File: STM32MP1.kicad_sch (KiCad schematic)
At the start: 1 part, among them U2 EMMC04G-S100-B08U

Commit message: added mmc schematic
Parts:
- removed U2: EMMC04G-S100-B08U, EMMC04G-S100-B08U:MICRON_EMMC_153-12, symbol EMMC04G-S100-B08U:EMMC04G-S100-B08U
- added J1: Micro_SD_Card_Det1, microSD:J_SD_Card-micro_socket_A, symbol Connector:Micro_SD_Card_Det1
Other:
- added sheet EMMC (EMMC.kicad_sch)
- sheet STM32MP1_Processor ports: added EMMC[0..10], GND, VDD_DDR, VREF_DDR; removed none

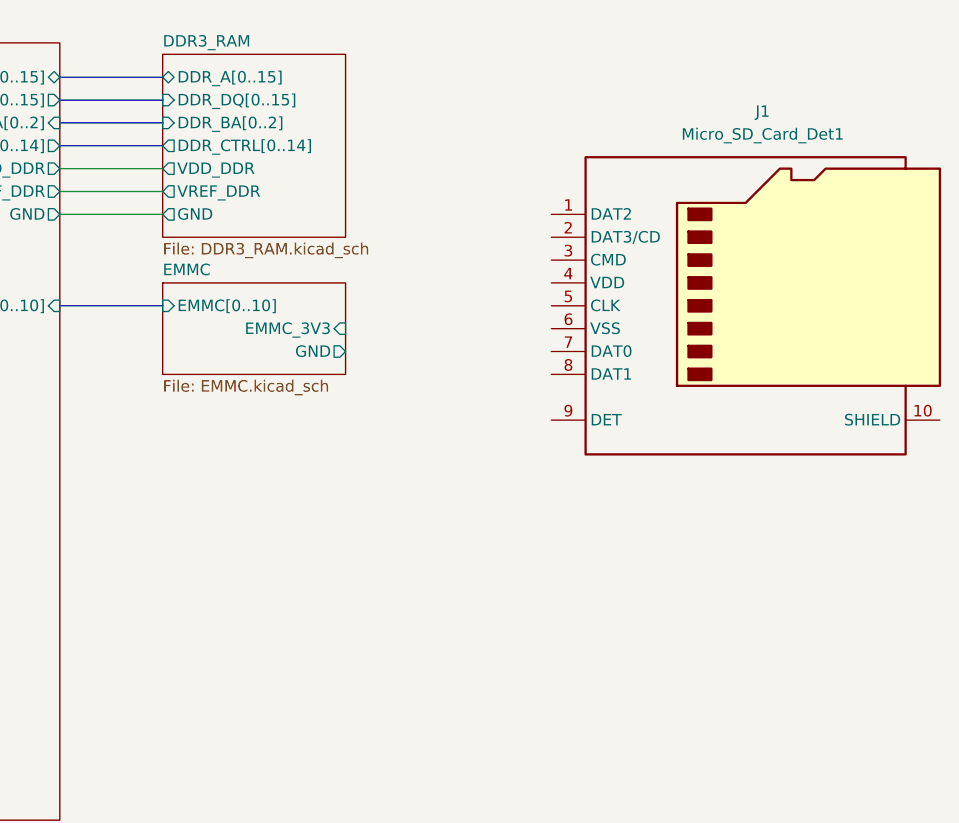
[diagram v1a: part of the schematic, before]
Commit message: Included Tushar's changed also added SDCARD module
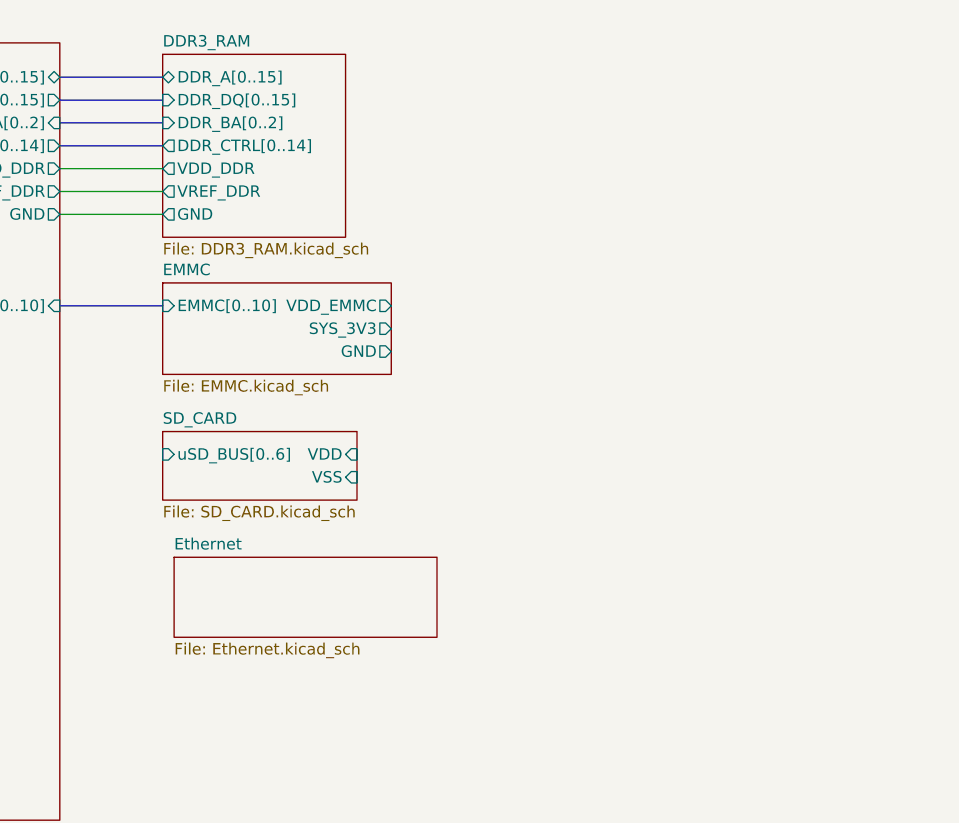
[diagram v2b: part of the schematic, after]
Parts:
- removed J1: Micro_SD_Card_Det1, microSD:J_SD_Card-micro_socket_A, symbol Connector:Micro_SD_Card_Det1
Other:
- added sheet Ethernet (Ethernet.kicad_sch)
- added sheet SD_CARD (SD_CARD.kicad_sch)
- sheet EMMC ports: added SYS_3V3, VDD_EMMC; removed EMMC_3V3
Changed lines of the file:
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@@
-		)
-	)
-	(symbol
-		(lib_id "Connector:Micro_SD_Card_Det1")
-		(at 214.63 67.31 0)
-		(unit 1)
-		(exclude_from_sim no)
-		(in_bom yes)
-		(on_board yes)
-		(dnp no)
-		(fields_autoplaced yes)
-		(property "Reference" "J1"
-			(at 215.265 45.72 0)
-			(effects
-				(font
-					(size 1.27 1.27)
-				)
-			)
-		)
-		(property "Value" "Micro_SD_Card_Det1"
-			(at 215.265 48.26 0)
-			(effects
-				(font
-					(size 1.27 1.27)
-				)
-			)
-		)
-		(property "Footprint" "microSD:J_SD_Card-micro_socket_A"
-			(at 266.7 49.53 0)
-			(effects
-				(font
-					(size 1.27 1.27)
-				)
-				(hide yes)
-			)
-		)
-		(property "Datasheet" "https://datasheet.lcsc.com/lcsc/2110151630_XKB-Connectivity-XKTF-015-N_C381082.pdf"
-			(at 214.63 64.77 0)
-			(effects
-				(font
-					(size 1.27 1.27)
-				)
-				(hide yes)
-			)
-		)
-		(property "Description" "Micro SD Card Socket with one card detection pin"
-			(at 214.63 67.31 0)
-			(effects
-				(font
-					(size 1.27 1.27)
-				)
-				(hide yes)
-			)
-		)
-		(pin "7"
-		)
-		(pin "9"
-		)
-		(pin "10"
-		)
-		(pin "8"
-		)
-		(pin "6"
-		)
-		(pin "1"
-		)
-		(pin "5"
-		)
-		(pin "4"
-		)
-		(pin "3"
-		)
-		(pin "2"
-		)
-		(instances
-			(project ""
-				(path "/d2fe1267-1d94-424f-9612-b5ac081691c8"
-					(reference "J1")
-					(unit 1)
-				)
-			)
 		)
 	)
 	(sheet
 		(at 148.59 64.77)
-		(size 20.32 10.16)
+		(size 25.4 10.16)
 		(exclude_from_sim no)
 		(in_bom yes)
@@
 			)
 		)
-		(pin "EMMC_3V3" input
-			(at 168.91 69.85 0)
-			(effects
-				(font
-					(size 1.27 1.27)
-				)
-				(justify right)
-			)
-		)
 		(pin "GND" output
-			(at 168.91 72.39 0)
+			(at 173.99 72.39 0)
 			(effects
 				(font
@@
 			)
 		)
+		(pin "VDD_EMMC" output
+			(at 173.99 67.31 0)
+			(effects
+				(font
+					(size 1.27 1.27)
+				)
+				(justify right)
+			)
+		)
+		(pin "SYS_3V3" output
+			(at 173.99 69.85 0)
+			(effects
+				(font
+					(size 1.27 1.27)
+				)
+				(justify right)
+			)
+		)
 		(instances
 			(project "STM32MP1"
@@
 				)
 			)
+		)
+	)
+	(sheet
+		(at 148.59 81.28)
+		(size 21.59 7.62)
+		(exclude_from_sim no)
+		(in_bom yes)
+		(on_board yes)
+		(dnp no)
+		(fields_autoplaced yes)
+		(stroke
+			(width 0.1524)
+			(type solid)
+		)
+		(fill
+			(color 0 0 0 0.0000)
+		)
+		(property "Sheetname" "SD_CARD"
+			(at 148.59 80.5684 0)
+			(effects
+				(font
+					(size 1.27 1.27)
+				)
+				(justify left bottom)
+			)
+		)
+		(property "Sheetfile" "SD_CARD.kicad_sch"
+			(at 148.59 89.4846 0)
+			(effects
+				(font
+					(size 1.27 1.27)
+				)
+				(justify left top)
+			)
+		)
+		(pin "VSS" input
+			(at 170.18 86.36 0)
+			(effects
+				(font
+					(size 1.27 1.27)
+				)
+				(justify right)
+			)
+		)
+		(pin "VDD" input
+			(at 170.18 83.82 0)
+			(effects
+				(font
+					(size 1.27 1.27)
+				)
+				(justify right)
+			)
+		)
+		(pin "uSD_BUS[0..6]" input
+			(at 148.59 83.82 180)
+			(effects
+				(font
+					(size 1.27 1.27)
+				)
+				(justify left)
+			)
+		)
+		(instances
+			(project "STM32MP1"
+				(path "/d2fe1267-1d94-424f-9612-b5ac081691c8"
+					(page "5")
+				)
+			)
+		)
+	)
+	(sheet
+		(at 149.86 95.25)
+		(size 29.21 8.89)
+		(exclude_from_sim no)
+		(in_bom yes)
+		(on_board yes)
+		(dnp no)
+		(fields_autoplaced yes)
+		(stroke
+			(width 0.1524)
+			(type solid)
+		)
+		(fill
+			(color 0 0 0 0.0000)
+		)
+		(property "Sheetname" "Ethernet"
+			(at 149.86 94.5384 0)
+			(effects
+				(font
+					(size 1.27 1.27)
+				)
+				(justify left bottom)
+			)
+		)
+		(property "Sheetfile" "Ethernet.kicad_sch"
+			(at 149.86 104.7246 0)
+			(effects
+				(font
+					(size 1.27 1.27)
+				)
+				(justify left top)
+			)
+		)
+		(instances
+			(project "STM32MP1"
+				(path "/d2fe1267-1d94-424f-9612-b5ac081691c8"
+					(page "6")
+				)
+			)

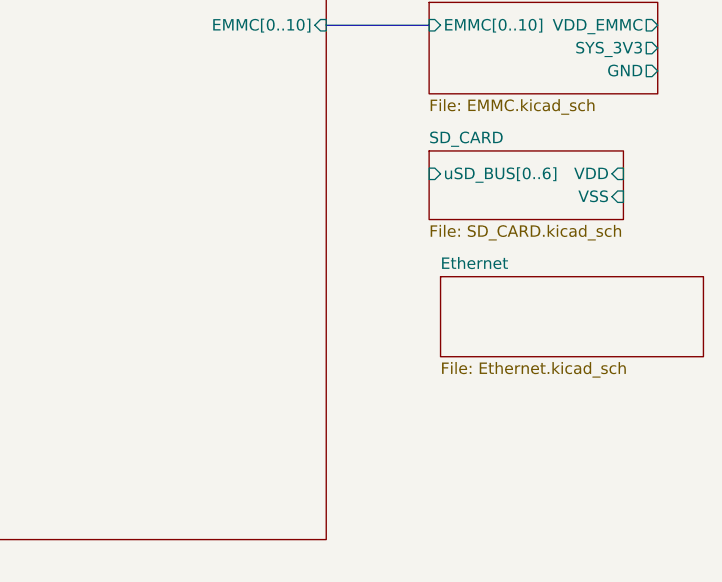
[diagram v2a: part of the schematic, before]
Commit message: Completed ETH Module as per ref schematic also populated compatible busses in processor module
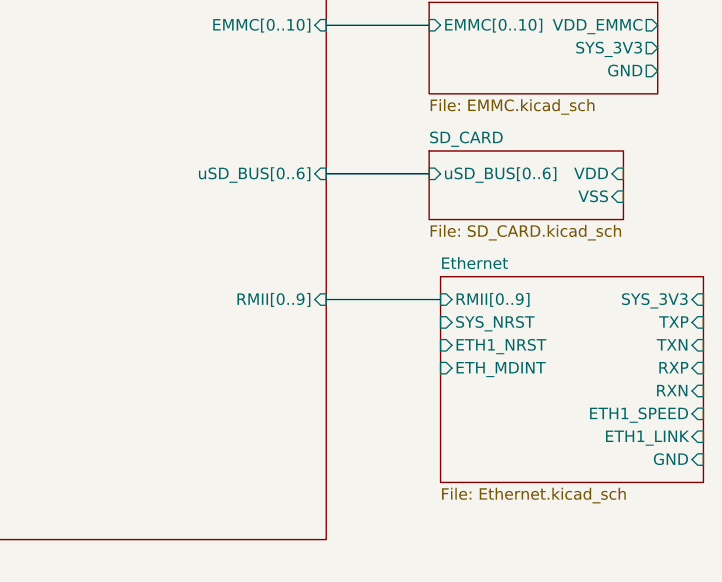
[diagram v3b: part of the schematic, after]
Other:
- sheet Ethernet ports: added ETH1_LINK, ETH1_NRST, ETH1_SPEED, ETH_MDINT, GND, RMII[0..9], RXN, RXP, SYS_3V3, SYS_NRST, TXN, TXP; removed none
- sheet STM32MP1_Processor ports: added RMII[0..9], uSD_BUS[0..6]; removed none
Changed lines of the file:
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@@
+		)
+	)
+	(bus
+		(pts
+			(xy 137.16 97.79) (xy 149.86 97.79)
+		)
+		(stroke
+			(width 0)
+			(type default)
 		)
 	)
@@
 		(pts
 			(xy 137.16 52.07) (xy 148.59 52.07)
+		)
+		(stroke
+			(width 0)
+			(type default)
+		)
+	)
+	(bus
+		(pts
+			(xy 137.16 83.82) (xy 148.59 83.82)
 		)
 		(stroke
@@
 			)
 		)
+		(pin "RMII[0..9]" input
+			(at 137.16 97.79 0)
+			(effects
+				(font
+					(size 1.27 1.27)
+				)
+				(justify right)
+			)
+		)
+		(pin "uSD_BUS[0..6]" input
+			(at 137.16 83.82 0)
+			(effects
+				(font
+					(size 1.27 1.27)
+				)
+				(justify right)
+			)
+		)
 		(instances
 			(project "STM32MP1"
@@
 	(sheet
 		(at 149.86 95.25)
-		(size 29.21 8.89)
+		(size 29.21 22.86)
 		(exclude_from_sim no)
 		(in_bom yes)
@@
 		)
 		(property "Sheetfile" "Ethernet.kicad_sch"
-			(at 149.86 104.7246 0)
+			(at 149.86 118.6946 0)
 			(effects
 				(font
@@
 			)
 		)
+		(pin "RXN" input
+			(at 179.07 107.95 0)
+			(effects
+				(font
+					(size 1.27 1.27)
+				)
+				(justify right)
+			)
+		)
+		(pin "SYS_NRST" input
+			(at 149.86 100.33 180)
+			(effects
+				(font
+					(size 1.27 1.27)
+				)
+				(justify left)
+			)
+		)
+		(pin "RXP" input
+			(at 179.07 105.41 0)
+			(effects
+				(font
+					(size 1.27 1.27)
+				)
+				(justify right)
+			)
+		)
+		(pin "GND" input
+			(at 179.07 115.57 0)
+			(effects
+				(font
+					(size 1.27 1.27)
+				)
+				(justify right)
+			)
+		)
+		(pin "TXP" input
+			(at 179.07 100.33 0)
+			(effects
+				(font
+					(size 1.27 1.27)
+				)
+				(justify right)
+			)
+		)
+		(pin "TXN" input
+			(at 179.07 102.87 0)
+			(effects
+				(font
+					(size 1.27 1.27)
+				)
+				(justify right)
+			)
+		)
+		(pin "RMII[0..9]" input
+			(at 149.86 97.79 180)
+			(effects
+				(font
+					(size 1.27 1.27)
+				)
+				(justify left)
+			)
+		)
+		(pin "ETH1_NRST" input
+			(at 149.86 102.87 180)
+			(effects
+				(font
+					(size 1.27 1.27)
+				)
+				(justify left)
+			)
+		)
+		(pin "SYS_3V3" input
+			(at 179.07 97.79 0)
+			(effects
+				(font
+					(size 1.27 1.27)
+				)
+				(justify right)
+			)
+		)
+		(pin "ETH1_LINK" input
+			(at 179.07 113.03 0)
+			(effects
+				(font
+					(size 1.27 1.27)
+				)
+				(justify right)
+			)
+		)
+		(pin "ETH_MDINT" input
+			(at 149.86 105.41 180)
+			(effects
+				(font
+					(size 1.27 1.27)
+				)
+				(justify left)
+			)
+		)
+		(pin "ETH1_SPEED" input
+			(at 179.07 110.49 0)
+			(effects
+				(font
+					(size 1.27 1.27)
+				)
+				(justify right)
+			)
+		)

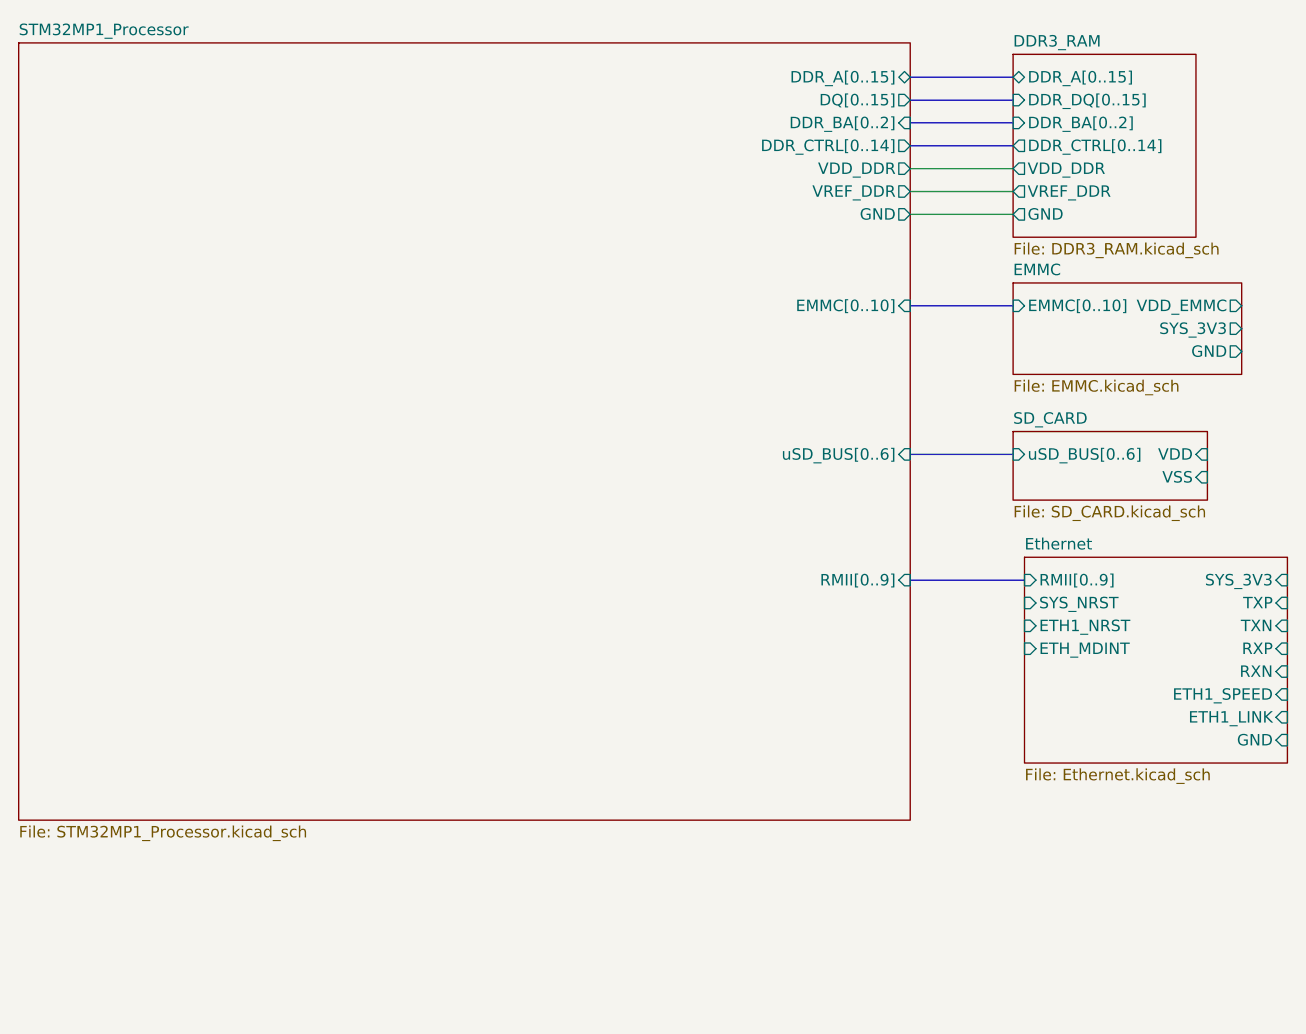
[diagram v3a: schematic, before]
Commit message: Added PMIC, WIFI and updated to STM32MP157 design
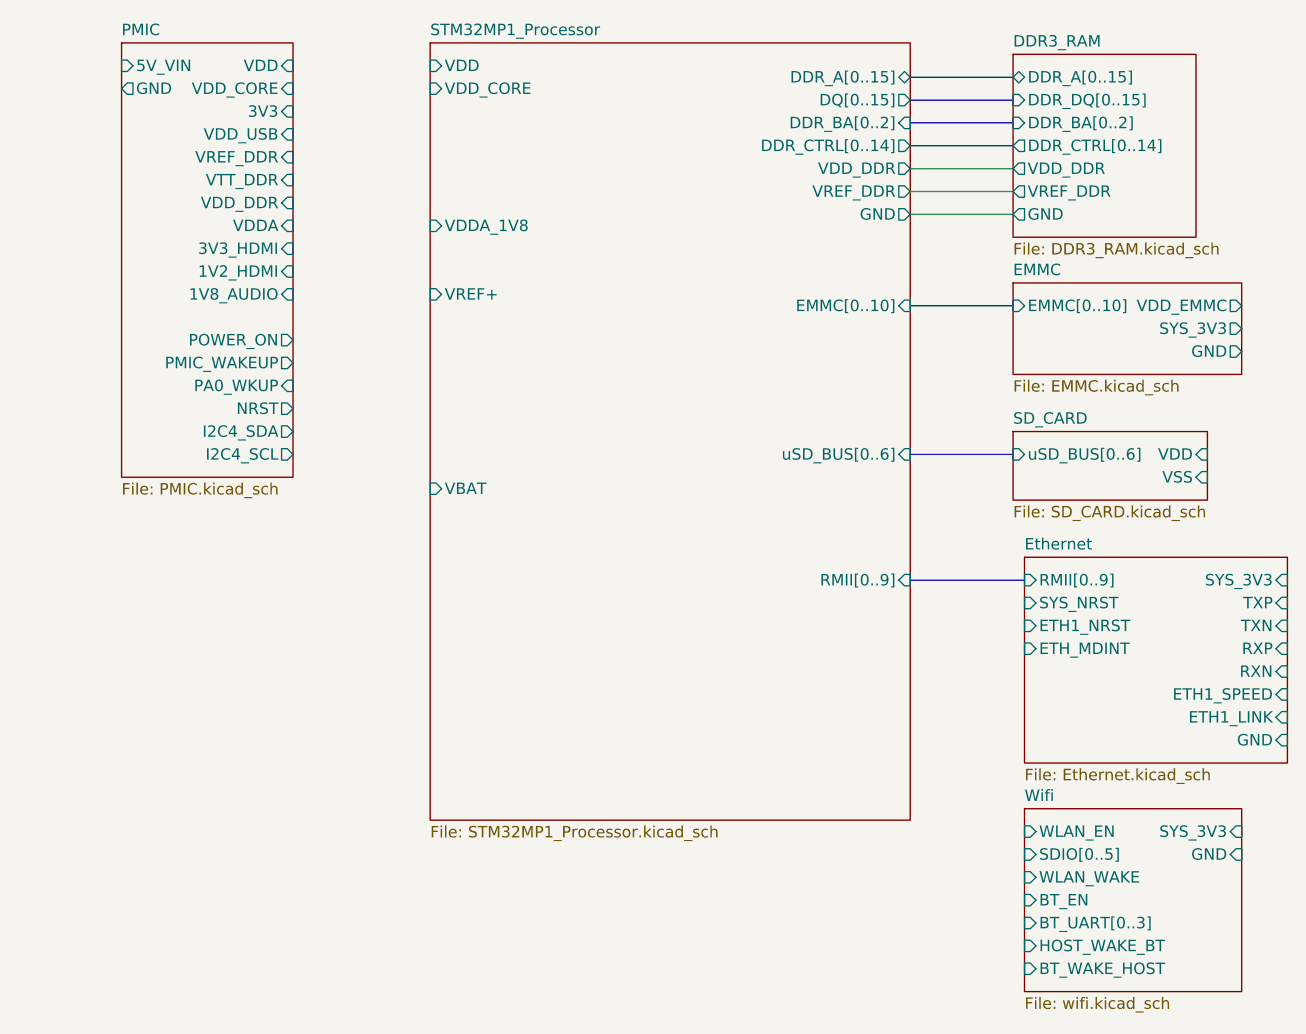
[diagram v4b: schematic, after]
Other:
- added sheet PMIC (PMIC.kicad_sch)
- added sheet Wifi (wifi.kicad_sch)
- sheet STM32MP1_Processor ports: added VBAT, VDD, VDDA_1V8, VDD_CORE, VREF+; removed none
